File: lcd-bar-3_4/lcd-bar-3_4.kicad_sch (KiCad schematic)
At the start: 32 parts, among them J1 SWD, J2 Conn_01x40_MountingPin, SW1 BOOT0, SW2 RST, U1 siplex-som-s16, U2 TPS61169

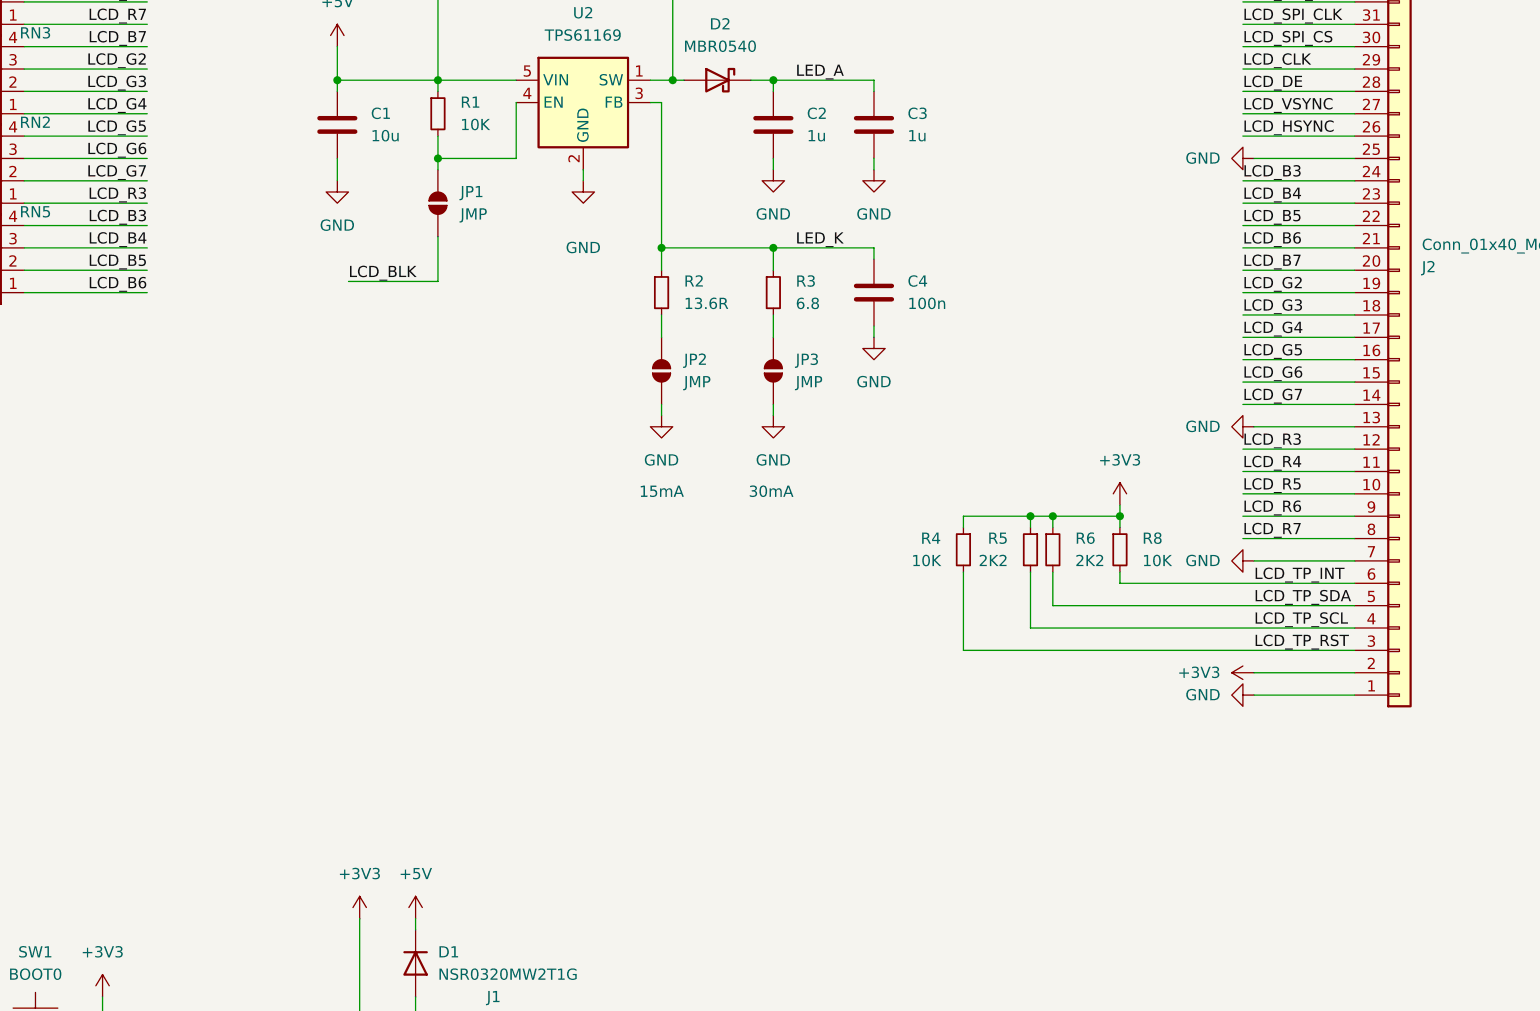
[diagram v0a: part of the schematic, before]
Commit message: Add LCD square 4-inch 480-480 & 720-720
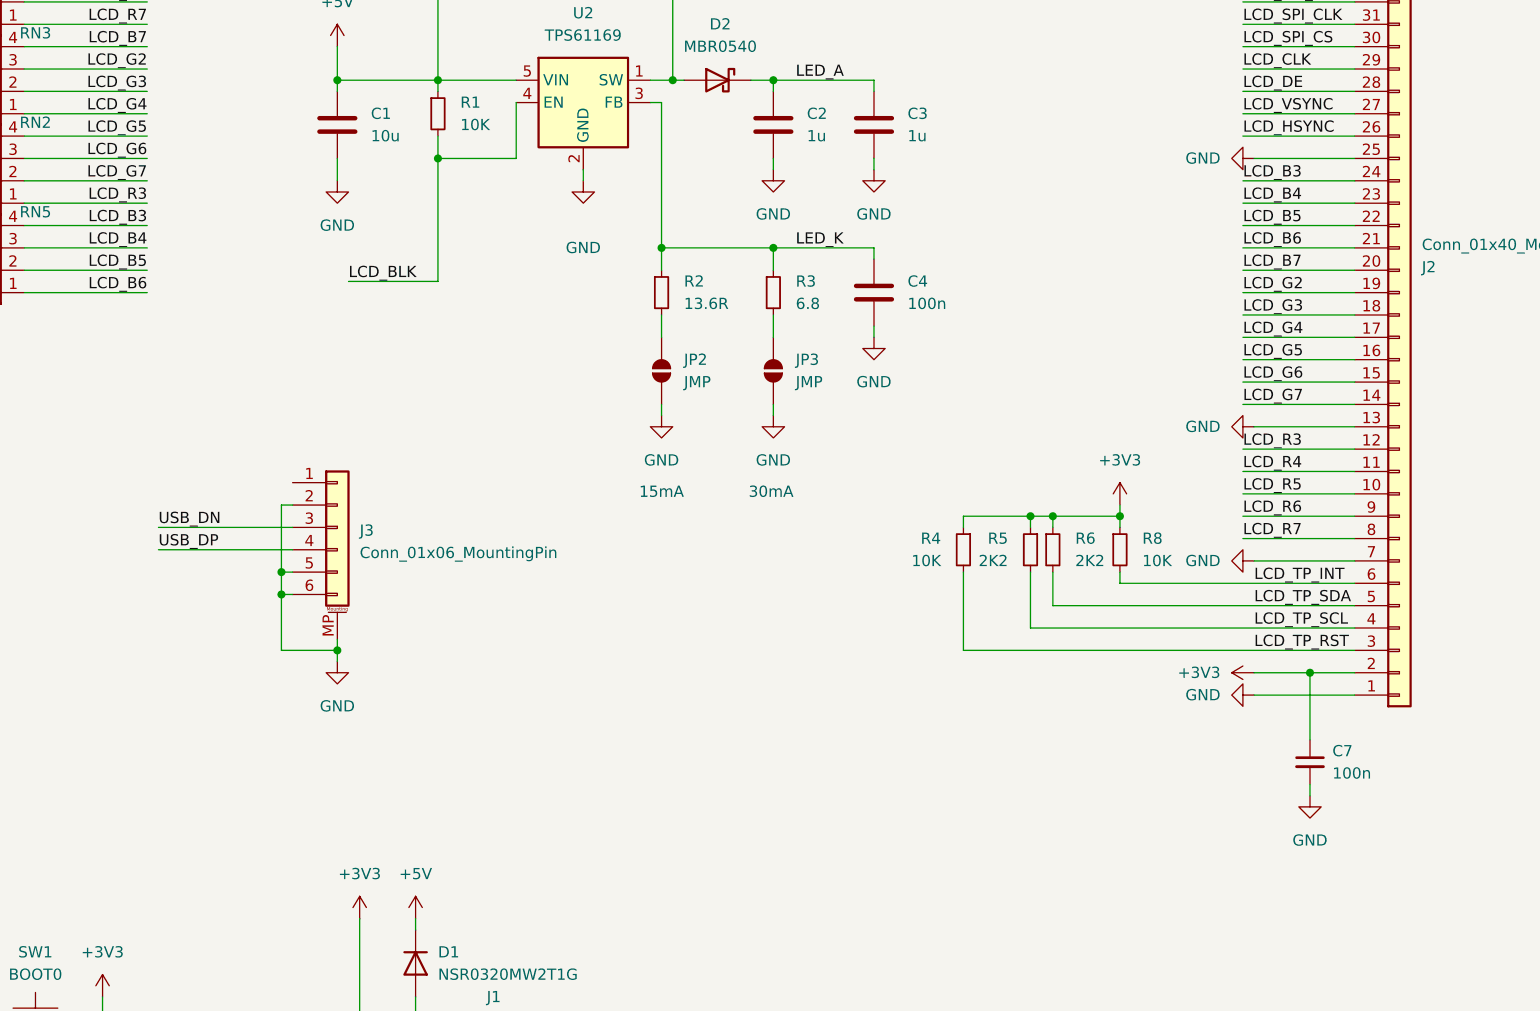
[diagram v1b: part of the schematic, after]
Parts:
- removed JP1: JMP, Jumper:SolderJumper-2_P1.3mm_Open_RoundedPad1.0x1.5mm, symbol Jumper:SolderJumper_2_Open
- added C7: 100n, Capacitor_SMD:C_0603_1608Metric, symbol Device:C_Small
- added J3: Conn_01x06_MountingPin, Connector_FFC-FPC:Hirose_FH12-6S-0.5SH_1x06-1MP_P0.50mm_Horizontal, symbol Connector_Generic_MountingPin:Conn_01x06_MountingPin
- C2, C3: footprint Capacitor_SMD:C_0402_1005Metric -> Capacitor_SMD:C_0603_1608Metric
- R4, R5, R6, R7, R8: footprint Inductor_SMD:L_0603_1608Metric_Pad1.05x0.95mm_HandSolder -> Resistor_SMD:R_0402_1005Metric
- RN1, RN2, RN3, RN4, RN5: footprint Resistor_SMD:R_Array_Convex_4x0603 -> Resistor_SMD:R_Array_Convex_4x0402
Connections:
- net +3V3: now also C7.1
- net GND: now also C7.2, J3.2 (Pin_2), J3.5 (Pin_5), J3.6 (Pin_6), J3.MP (MountPin)
- net LCD_BLK: now also R1.2, U2.4 (EN)
- net USB_DN: now also J3.3 (Pin_3)
- net USB_DP: now also J3.4 (Pin_4)

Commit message: 98% finished, st-link part left
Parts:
- added J4: Conn_01x10_MountingPin, Connector_Molex:Molex_PicoBlade_53261-1071_1x10-1MP_P1.25mm_Horizontal, symbol Connector_Generic_MountingPin:Conn_01x10_MountingPin
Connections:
- net +5V: now also J4.1 (Pin_1), J4.2 (Pin_2); no longer R1.1
- net GND: now also R1.2, J4.3 (Pin_3), J4.4 (Pin_4), J4.5 (Pin_5), J4.MP (MountPin)
- net LCD_BLK: now also R1.1, U1.16 (PB0); no longer R1.2
- net LCD_RST: now also U1.36 (PI3); no longer U1.1 (PB7)
- net LCD_SPI_CS: now also U1.38 (PC12); no longer U1.40 (PB4)
- net LCD_SPI_DAT: now also U1.35 (PD7); no longer U1.88 (PB5)
- net LCD_TP_INT: now also U1.1 (PB7); no longer U1.4 (PH4)
- net LCD_TP_RST: now also U1.4 (PH4); no longer U1.6 (PC0)
- net SW: now reaches D2.2 (A), L1.2, U2.1 (SW)
- net PWR_BTN: now reaches U1.10 (PA1)
- net PWR_BTN: now also J4.10 (Pin_10)
- net EE_SCL: now reaches U1.20 (PB10)
- net EE_SDA: now reaches U1.22 (PB11)
- net SERIAL_TX: now reaches U1.23 (PB14)
- net SERIAL_TX: now also J4.8 (Pin_8)
- net SERIAL_RX: now reaches U1.24 (PB15)
- net SERIAL_RX: now also J4.7 (Pin_7)
- net PWR_LED: now reaches U1.9 (PA0)
- net PWR_LED: now also J4.9 (Pin_9)
- new net AUX_IO: J4.6 (Pin_6), U1.6 (PC0)
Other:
- moved on the sheet: R1

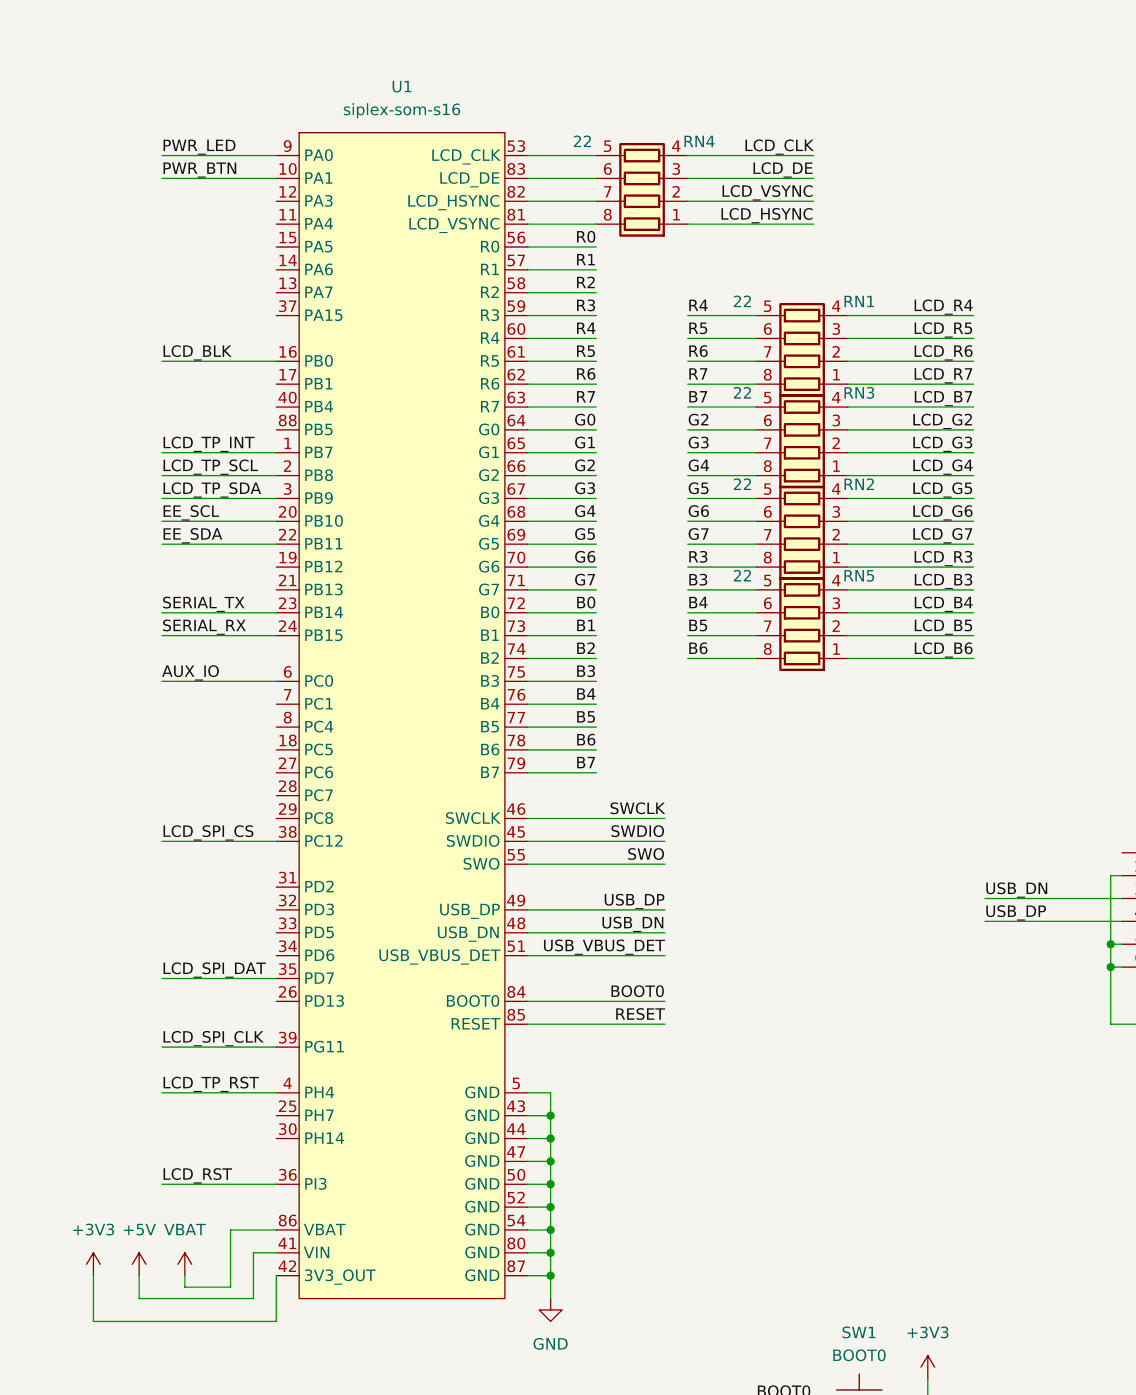
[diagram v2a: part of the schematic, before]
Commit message: Add LCD standard 7inch
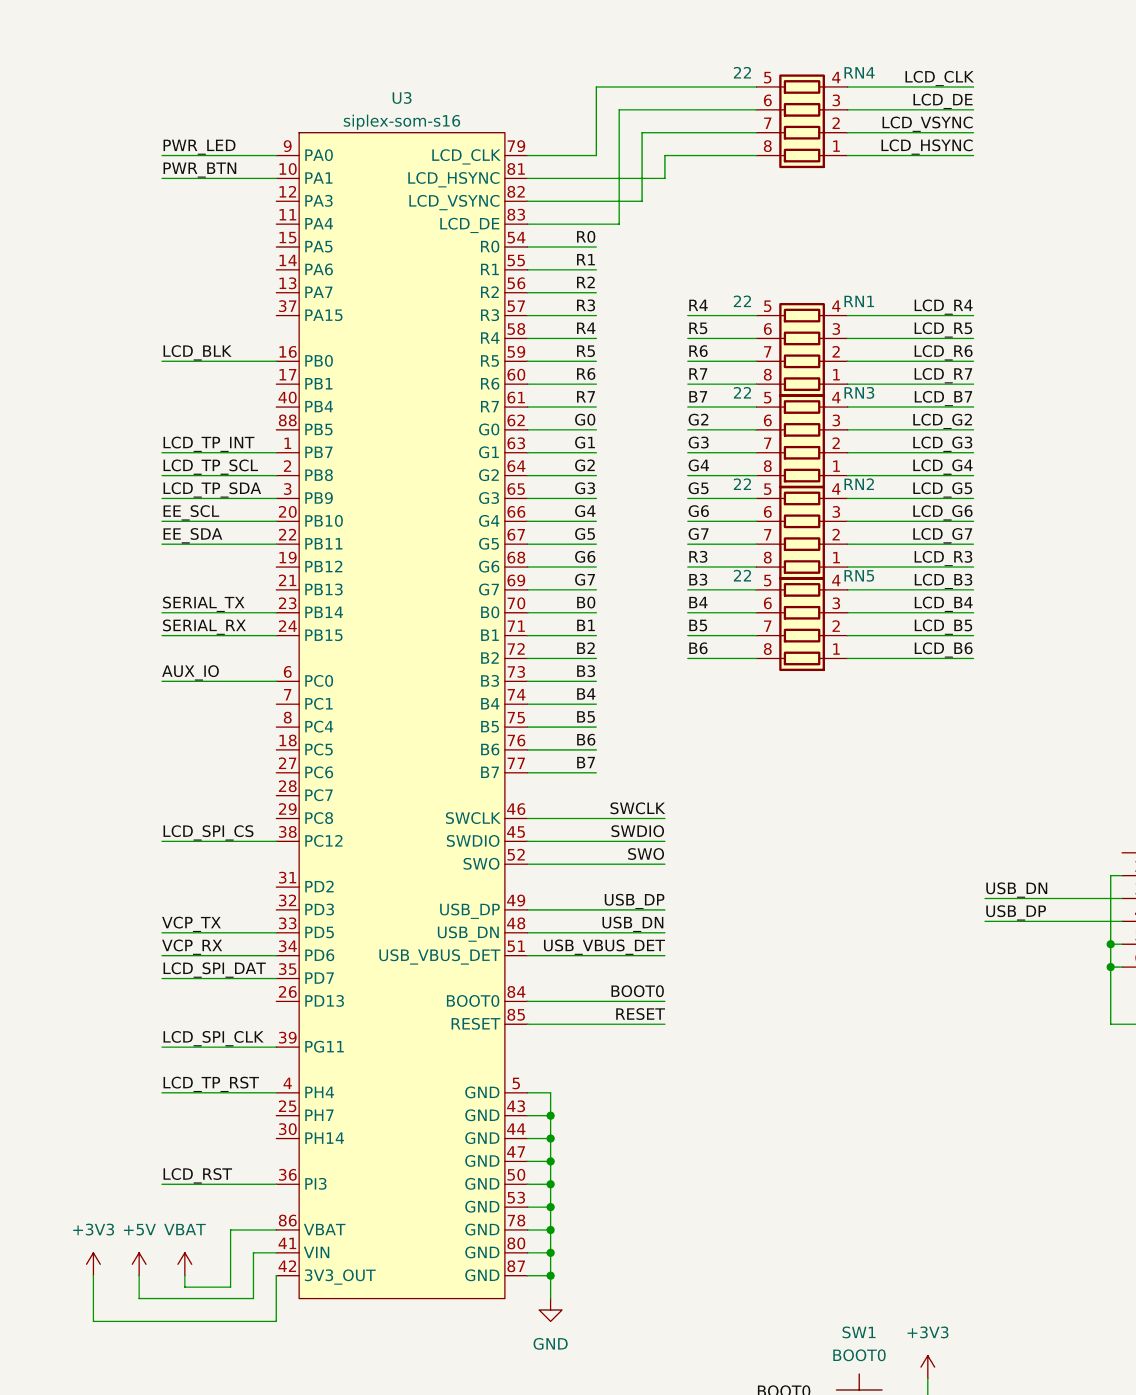
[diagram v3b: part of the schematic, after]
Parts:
- removed U1: siplex-som-s16, siplex:siplex-som-s16, symbol siplex-som:siplex-som-s16
- added U3: siplex-som-s16, siplex:siplex-som-s16, symbol siplex-som:siplex-som-s16
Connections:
- net +3V3: now also U3.42 (3V3_OUT)
- net +5V: now also U3.41 (VIN)
- net AUX_IO: now also U3.6 (PC0)
- net B0: now also U3.70 (B0)
- net B1: now also U3.71 (B1)
- net B2: now also U3.72 (B2)
- net B3: now also U3.73 (B3)
- net B4: now also U3.74 (B4)
- net B5: now also U3.75 (B5)
- net B6: now also U3.76 (B6)
- net B7: now also U3.77 (B7)
- net BOOT0: now also U3.84 (BOOT0)
- net EE_SCL: now also U3.20 (PB10)
- net EE_SDA: now also U3.22 (PB11)
- net G0: now also U3.62 (G0)
- net G1: now also U3.63 (G1)
- net G2: now also U3.64 (G2)
- net G3: now also U3.65 (G3)
- net G4: now also U3.66 (G4)
- net G5: now also U3.67 (G5)
- net G6: now also U3.68 (G6)
- net G7: now also U3.69 (G7)
- net GND: now also U3.43 (GND), U3.44 (GND), U3.47 (GND), U3.5 (GND), U3.50 (GND), U3.53 (GND), U3.78 (GND), U3.80 (GND), U3.87 (GND)
- net LCD_BLK: now also U3.16 (PB0)
- net LCD_RST: now also U3.36 (PI3)
- net LCD_SPI_CLK: now also U3.39 (PG11)
- net LCD_SPI_CS: now also U3.38 (PC12)
- net LCD_SPI_DAT: now also U3.35 (PD7)
- net LCD_TP_INT: now also U3.1 (PB7)
- net LCD_TP_RST: now also U3.4 (PH4)
- net LCD_TP_SCL: now also U3.2 (PB8)
- net LCD_TP_SDA: now also U3.3 (PB9)
- net PWR_BTN: now also U3.10 (PA1)
- net PWR_LED: now also U3.9 (PA0)
- net R0: now also U3.54 (R0)
- net R1: now also U3.55 (R1)
- net R2: now also U3.56 (R2)
- net R3: now also U3.57 (R3)
- net R4: now also U3.58 (R4)
- net R5: now also U3.59 (R5)
- net R6: now also U3.60 (R6)
- net R7: now also U3.61 (R7)
- net RESET: now also U3.85 (RESET)
- net SERIAL_RX: now also U3.24 (PB15)
- net SERIAL_TX: now also U3.23 (PB14)
- net SWCLK: now also U3.46 (SWCLK)
- net SWDIO: now also U3.45 (SWDIO)
- net SWO: now also U3.52 (SWO)
- net USB_DN: now also U3.48 (USB_DN)
- net USB_DP: now also U3.49 (USB_DP)
- net USB_VBUS_DET: now also U3.51 (USB_VBUS_DET)
- net VBAT: now also U3.86 (VBAT)
- net VCP_RX: now also U3.34 (PD6)
- net VCP_TX: now also U3.33 (PD5)
- net at RN4.5 (R4.2): now also U3.79 (LCD_CLK)
- net at RN4.8 (R1.2): now also U3.81 (LCD_HSYNC)
- net at RN4.7 (R2.2): now also U3.82 (LCD_VSYNC)
- net at RN4.6 (R3.2): now also U3.83 (LCD_DE)
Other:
- moved on the sheet: RN4

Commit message: Slight changes
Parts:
- C1: footprint Capacitor_SMD:C_0603_1608Metric -> Capacitor_SMD:C_0805_2012Metric; JLCPCB Part # (none) -> C15850
- C2, C3: JLCPCB Part # (none) -> C15849
- C4: JLCPCB Part # (none) -> C1525
- C5: JLCPCB Part # (none) -> C15850
- C6, C7: footprint Capacitor_SMD:C_0603_1608Metric -> Capacitor_SMD:C_0402_1005Metric; JLCPCB Part # (none) -> C1525
- D1: JLCPCB Part # (none) -> C48192
- D2: JLCPCB Part # (none) -> C7420330
- FB1: JLCPCB Part # (none) -> C1017
- J1: JLCPCB Part # (none) -> C5160763C5160763
- J2: JLCPCB Part # (none) -> C225713
- L1: value 6.8u -> 4.7u; JLCPCB Part # (none) -> C57269
- R1, R4, R7, R8: JLCPCB Part # (none) -> C25744
- R2: value 13.6R -> 13.7R; JLCPCB Part # (none) -> C482772
- R3: JLCPCB Part # (none) -> C228038
- R5, R6: JLCPCB Part # (none) -> C25879
- RN1, RN2, RN3, RN4, RN5: value 22 -> 100; JLCPCB Part # (none) -> C48442
- SW1, SW2: JLCPCB Part # (none) -> C127488
- U2: JLCPCB Part # (none) -> C71045
- U3: now left out of the parts list
